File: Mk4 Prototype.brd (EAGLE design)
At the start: 121.6 x 80 mm, 223 parts, among them IC1 MSP432E401, IC10 TPD3E001DRL, IC11 LMV358ID, IC12 SN74HC4066D, IC13 TPA2006D1, IC2 AS4C4M16SA-7TCN, IC3 CC3120MOD, IC4 MCP23017ML, IC5 SIM800C, IC6 SST26VF016B-104I/SM, IC7 TPD3E001DRL, IC8 BQ25601, IC9 TPS62082, J1 78723-1001, J2 ER-CON50HT-1, J3 2x5 1.27mm, J4 GSM-COIL-ANT, J5 S2B-PH-SM4-TB(LF)(SN), Q1 2N7002PW, Q2 2N7002PW, Q3 CSD25402Q3A, Q8 CSD13202Q2, SW1 JOYSTICK, U1 ZX62-B-5PA(33), U4 MIC-4MM, U5 LDMS1540S-01-R8-0.8-R, X1 ABS07-32.768KHZ-T, X2 ABM8G-25.000MHZ-B4Y-T

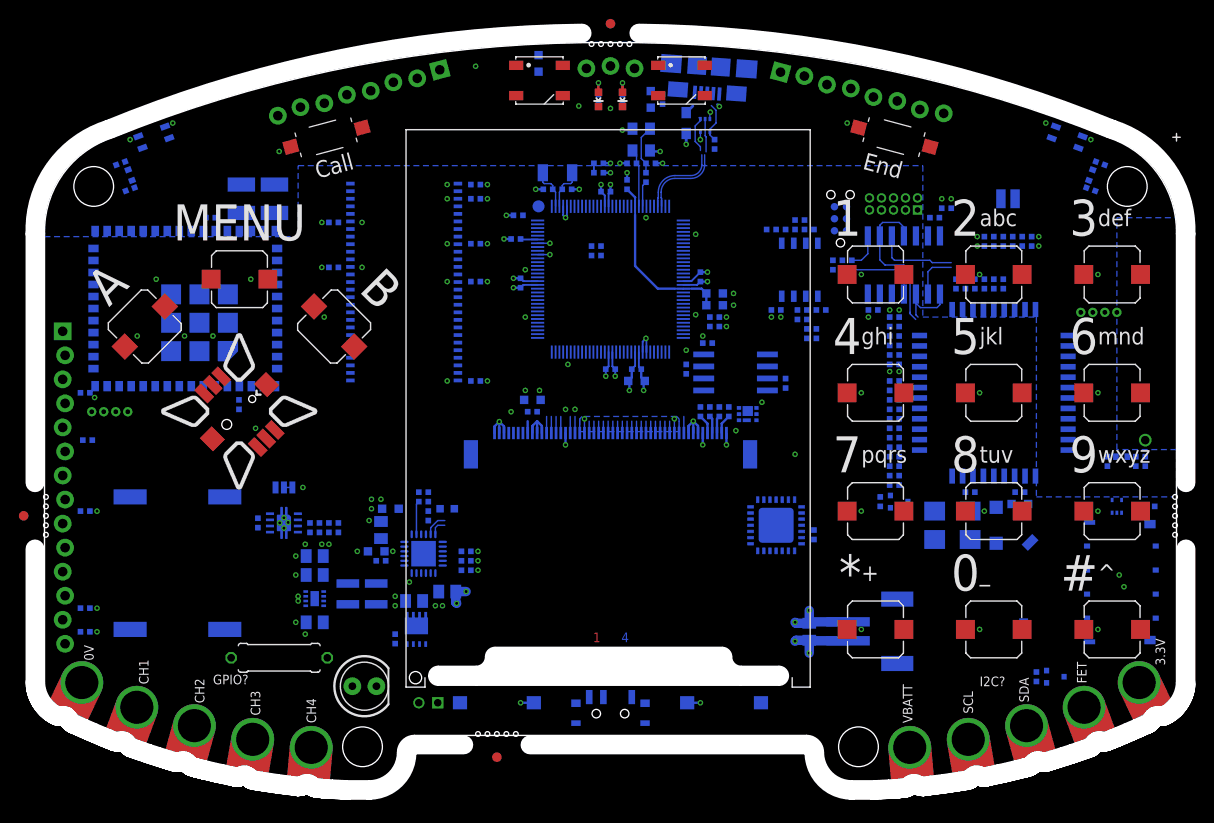
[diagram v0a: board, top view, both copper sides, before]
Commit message: Bom based updates
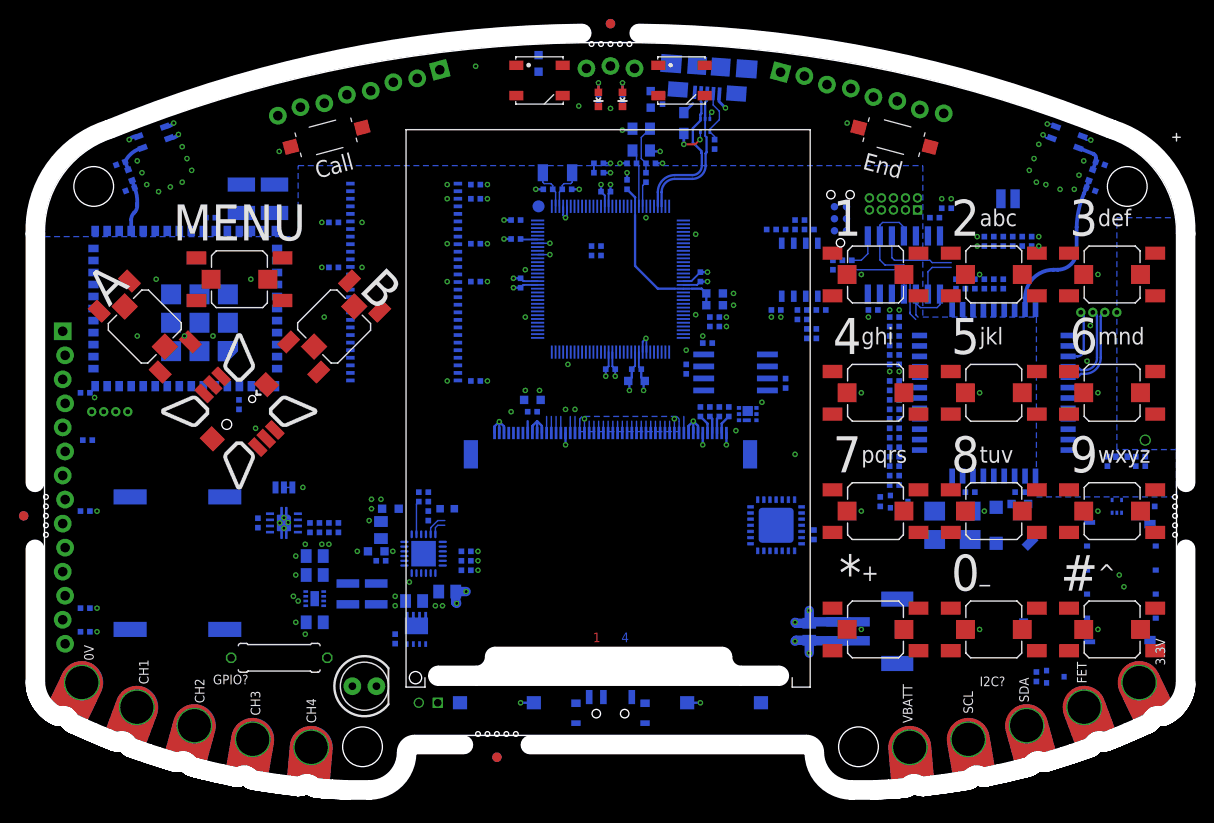
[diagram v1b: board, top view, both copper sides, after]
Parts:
- C1, C14, C41, C7: value 0603/1u/10V/X5R -> 0603/1u/6V3/X5R
- C20: value 0603/3300p/50V/X7R -> 0603/3n3/50V/X7R
- C48, C49, C50: value 0402/22p/10V/X5R -> 0402/22p/10V/C0G
- C52, C54, C55, C64, C66, C67: value 0402/33p/50V/X5R -> 0402/33p/50V/C0G
- C53, C56, C57, C65, C68, C69: value 0402/10p/50V/X5R -> 0402/10p/50V/C0G
- C6: value 0603/2u2/10V/X5R -> 0603/2u2/6V3/X5R
- S1, S10, S11, S12, S13, S14, S15, S2, S3, S4, S5, S6, S7, S8, S9: device TiLDA Mk4 Parts:SKPMAPE010 -> TiLDA Mk4 Parts:SKPMAPE010-COMBINED
- moved C52 1.00 mm to (42.0, 57.5)
- moved C53 1.00 mm to (40.0, 56.5)
- moved C54 1.00 mm to (44.0, 57.5)
- moved C55 1.00 mm to (40.0, 57.5)
- moved C56 1.00 mm to (42.0, 56.5)
- moved C57 1.00 mm to (44.0, 56.5)
- moved R5 0.56 mm to (-10.0, 59.2)
- moved L2 0.25 mm to (7.75, 69.5)
- turned S13 to 135 degrees
- turned S15 to 45 degrees
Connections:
- net N$1 renamed LED5_R
- net N$10 renamed AMP_IN_N
- net N$11 renamed AMP_IN_P
- net N$12 renamed AMP_IN_R_P
- net N$13 renamed BQ_STAT_R
- net N$14 renamed POWER_SWITCH
- net N$15 renamed AMP_IN_R_N
- net N$17 renamed BTST
- net N$19 renamed BQ_!QON
- net N$2 renamed MIC_PWM_AMP_+
- net N$3 renamed ETHLED0_R
- net N$4 renamed ETHLED1_R
- net N$5 renamed RBIAS+
- net N$51 renamed LED2_R
- net N$52 renamed LED1_R
- net N$6 renamed USB_SHIELD
- net N$64 renamed LEDK
- net N$7 renamed MIC_PWM_R
- net BTN_1: now also S1.B1, S1.B2
- net BTN_10: now also S10.B1, S10.B2
- net BTN_11: now also S11.B1, S11.B2
- net BTN_12: now also S12.B1, S12.B2
- net BTN_2: now also S2.B1, S2.B2
- net BTN_3: now also S3.B1, S3.B2
- net BTN_4: now also S4.B1, S4.B2
- net BTN_5: now also S5.B1, S5.B2
- net BTN_6: now also S6.B1, S6.B2
- net BTN_7: now also S7.B1, S7.B2
- net BTN_8: now also S8.B1, S8.B2
- net BTN_9: now also S9.B1, S9.B2
- net BTN_A: now also S13.B1, S13.B2
- net BTN_B: now also S15.B1, S15.B2
- net BTN_MENU: now also S14.B1, S14.B2
- net GND: now also S1.A1, S1.A2, S10.A1, S10.A2, S11.A1, S11.A2, S12.A1, S12.A2, S13.A1, S13.A2, S14.A1, S14.A2, S15.A1, S15.A2, S2.A1, S2.A2, S3.A1, S3.A2, S4.A1, S4.A2, S5.A1, S5.A2, S6.A1, S6.A2, S7.A1, S7.A2, S8.A1, S8.A2, S9.A1, S9.A2
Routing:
- net BT_ANT: track 0.00 -> 16.3 mm
- net SIM_D_N: track 0.00 -> 9.28 mm
- net SIM_D_P: track 0.00 -> 8.72 mm
- net GND: track 72.5 -> 80.1 mm, vias 106 -> 128
- net SIM_VBUS: track 0.00 -> 6.05 mm
- net WIFI_ANT: track 0.00 -> 5.54 mm
- net BT_ANT_L: track 0.00 -> 3.50 mm
- net USB_D_N: track 12.4 -> 15.8 mm
- net USB_D_P: track 11.9 -> 15.2 mm
- net WFIF_ANT_L: track 0.00 -> 3.26 mm
- net VBUS: track 1.98 -> 3.90 mm
- net USB_ID_R: track 4.28 -> 5.75 mm

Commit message: Connect some pins, try out TI Booster pack headers and add MIC disconnect
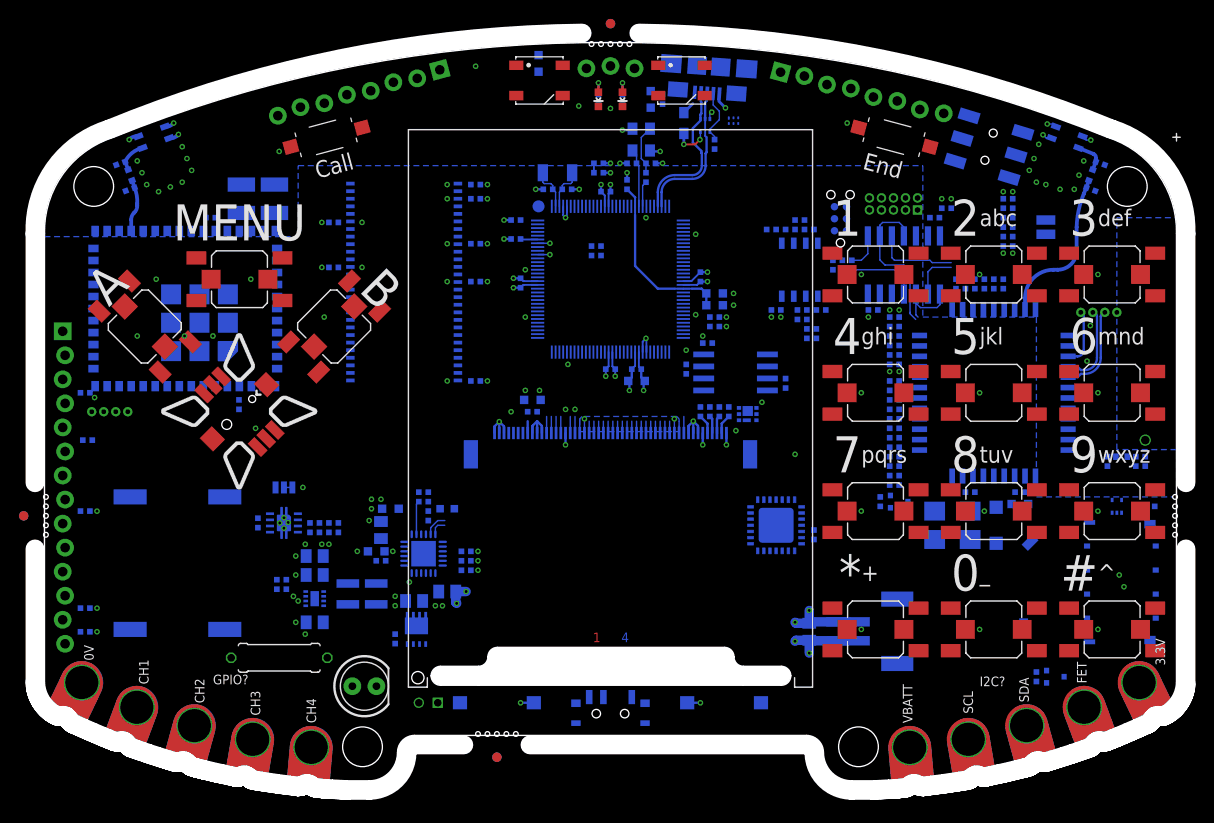
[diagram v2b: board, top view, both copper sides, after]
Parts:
- added IC14: TPD4S012, TiLDA Mk4 Parts:SON-6
- added R60, R61: (no value), TiLDA Mk4 Parts:R0402-SMALLER
- added S22: AYZ0202AGRLC, TiLDA Mk4 Parts:AYZ-JS-COMBINED
- moved U4 5.00 mm to (46.0, 58.5), turned to 90 degrees
- moved C53 4.74 mm to (41.5, 61.0), turned to 90 degrees
- moved C55 4.30 mm to (42.5, 61.0), turned to 90 degrees
- moved C56 2.55 mm to (41.5, 59.0), turned to 90 degrees
- moved C57 2.55 mm to (41.5, 57.0), turned to 270 degrees
- moved C52 1.58 mm to (42.5, 59.0), turned to 90 degrees
- moved C54 1.58 mm to (42.5, 57.0), turned to 270 degrees
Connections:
- net PD0 renamed CC_MISO
- net PD1 renamed CC_MOSI
- net PD2 renamed CC_!CS
- net PD3 renamed CC_CLK
- net PD4 renamed CC_TX
- net PD5 renamed CC_RX
- net PE1 renamed CC_!HIB
- net PJ0 renamed SIM_TX
- net PJ1 renamed SIM_RX
- net PK0 renamed CC_!RST
- removed net PA0: IC1.33
- removed net PA1: IC1.34
- removed net PD7: IC1.128
- removed net PE0: IC1.15
- removed net PE4: IC1.123
- removed net PE5: IC1.124
- removed net PF3: IC1.45
- removed net PN1: IC1.108
- removed net PN2: IC1.109
- removed net PP4: IC1.105
- removed net PP5: IC1.106
- removed net PQ4: IC1.102
- new net MIC_SWITCHED_N: IC12.10, S22.5
- new net MIC_SWITCHED_P: IC12.2, S22.2
- new net TPS_FB: IC9.4, R60.2, R61.1
- new net VCC: IC14.4
- net 3V3: now also R60.1
- net BQ_!INT: now also IC1.124
- net BTN_MENU: now also IC1.34
- net CC_IRQ: now also IC1.15
- net GND: now also IC14.6, R61.2
- net MCP_INT: now also IC1.33
- net MIC_N: now also S22.6; no longer IC12.10
- net MIC_P: now also S22.3; no longer IC12.2
- net MIC_PWM: now also IC1.45
- net MUX_A: now also IC1.108
- net MUX_B: now also IC1.109
- net NETLIGHT: now also IC1.105
- net PWR_KEY: now also IC1.106
- net SIM_STATUS: now also IC1.102
- net SPK_ADC: now also IC1.128
- net WS2812: now also IC1.123
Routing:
- net MIC_SWITCHED_N: track 0.00 -> 8.79 mm
- net MIC_N: track 8.79 -> 0.00 mm
- net MIC_SWITCHED_P: track 0.00 -> 5.01 mm
- net MIC_P: track 5.01 -> 0.00 mm
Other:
- board text added: "MIC"

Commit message: Night 4, Swap out CC3120MOD for CC3130R Getting some routing done
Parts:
- added C100, C101, C98, C99: 0402/12p/50V/C0G, TiLDA Mk4 Parts:C0402-SMALLER
- added C59, C60, C61, C62, C91, C92, C94, C95, C96, C97: 0402/100n/10V/X5R, TiLDA Mk4 Parts:C0402-SMALLER
- added C63, C87, C93: 0805/10u/10V/X5R, TiLDA Mk4 Parts:C0805-N
- added C84, C85: 0603/22u/4V/X5R, TiLDA Mk4 Parts:C0603K-SMALL
- added C86: 0402/1u/10V/X5R, TiLDA Mk4 Parts:C0402-SMALLER
- added C88, C89, C90: 0603/4u7/10V/X5R, TiLDA Mk4 Parts:C0603K-SMALL
- added FL1: DEA202450BT-1294C1-H, TiLDA Mk4 Parts:DEA202450BT
- added IC15: CC3120R, TiLDA Mk4 Parts:VQFN-64
- added L7, L9: LQM2HPN2R2MG0L, TiLDA Mk4 Parts:1008
- added L8: LQM2HPN1R0MG0L, TiLDA Mk4 Parts:1008
- added R62, R66: 0402/10K/5%, TiLDA Mk4 Parts:R0402-SMALLER
- added R63, R64, R65, R67, R68, R69, R70, R71, R72, R73: 0402/100K/5%, TiLDA Mk4 Parts:R0402-SMALLER
- added X3: ABS07-32.768KHZ-T, TiLDA Mk4 Parts:RESONATOR_EPSON_FC_145
- added X4: ABM8G-40.000MHZ-4Y-T3, TiLDA Mk4 Parts:CRYSTAL-3.2-2.5
- ANT1: device TiLDA Mk4 Parts:2450AT18D0100-RIGHT -> TiLDA Mk4 Parts:2450AT18D0100
- IC3: value CC3120MOD -> MX25R1635FM1IL0; device TiLDA Mk4 Parts:CC3100MOD-LWK -> TiLDA Mk4 Parts:SO08-EIAJ
- IC4: value MCP23017ML -> TCA9555; device TiLDA Mk4 Parts:QFN28-ML_6X6MM -> TiLDA Mk4 Parts:QFN-24
- moved R23 60.5 mm to (39.2, 11.8), turned to 90 degrees
- moved R24 59.1 mm to (38.2, 11.8), turned to 90 degrees
- moved ANT1 49.8 mm to (-58.4, 19.2), turned to 270 degrees
- moved C43 48.5 mm to (-37.8, 13.0), turned to 0 degrees
- moved C77 42.1 mm to (-57.5, 23.5), turned to 270 degrees
- moved L6 41.3 mm to (-56.0, 23.0), turned to 0 degrees
- moved C76 39.2 mm to (-54.2, 23.5), turned to 270 degrees
- moved SJ1 31.2 mm to (-31.0, 62.0), turned to 180 degrees
- moved U5 30.1 mm to (-44.0, 53.0)
- moved C44 29.5 mm to (-45.8, 30.2), turned to 90 degrees
- moved C58 27.1 mm to (-34.5, 54.2)
- moved IC3 25.4 mm to (-29.5, 29.8)
- moved JP8 25.1 mm to (-49.2, 14.0), flipped to the top, turned to 180 degrees
- moved C42 24.3 mm to (-34.0, 37.2)
- moved R25 23.4 mm to (-35.0, 16.8), turned to 180 degrees
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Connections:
- net LCD_BLIGHT renamed PWM0_LCD_BLIGHT
- net LCD_CLK renamed SSI0_LCD_CLK
- net LCD_CS renamed SSI0_LCD_CS
- net LCD_MISO renamed SSI0_LCD_MISO
- net LCD_MOSI renamed SSI0_LCD_MOSI
- net MIC_PWM renamed PWM3_MIC_PWM
- net NETLIGHT renamed SIM_NETLIGHT
- net PD6 renamed AIN5_PD6
- net PWR_KEY renamed SIM_PWR_KEY
- net SPK_ADC renamed AIN4_SPK_ADC
- removed net !CC_HIB: IC3.4, R25.1
- removed net !CC_RST: IC3.35
- removed net ADC_X: J2.46
- removed net ADC_Y: J2.47
- removed net CC_!CS: IC1.3
- removed net CC_!RST: IC1.18
- removed net CC_CLK: IC1.4
- removed net CC_MISO: IC1.1
- removed net CC_MOSI: IC1.2
- removed net CC_RX: IC1.126
- removed net CC_TX: IC1.125
- removed net PE2: IC1.13
- removed net PE3: IC1.12
- removed net PF1: IC1.43
- removed net PF2: IC1.44
- removed net PK7: IC1.60
- removed net PL4: IC1.85
- removed net PM6: IC1.72
- removed net SPI1_MISO: IC3.7
- removed net SPI1_MOSI: IC3.6
- removed net SPI1_NSS: IC3.8
- removed net SPI1_SCK: IC3.5
- removed net SSI3DAT3: IC1.119
- removed net USART1_RX: IC3.46
- removed net USART1_TX: IC3.47
- new net AIN0_ADC_X: IC1.13, J2.46
- new net AIN1_ADC_Y: IC1.12, J2.47
- new net CC_!CTS: IC15.61
- new net CC_!RESET: C60.2, IC1.18, IC15.32, R73.1
- new net CC_!RTS: IC15.50, R70.1
- new net CC_RCT_XTAL_N: C100.2, IC15.52, X3.P$1
- new net CC_RESERVED@19: IC15.19, R65.1
- new net CC_RTC_XTAL_P: C101.2, IC15.51, X3.P$2
- new net CC_WLAN_XTAL_: C99.2, IC15.22, X4.3
- new net CC_WLAN_XTAL_P: C98.2, IC15.23, X4.1
- new net DCDC_ANA2_SW_N: IC15.46
- new net DCDC_ANA2_SW_P: IC15.45
- new net DCDC_ANA_SW: IC15.38, L7.2
- new net DCDC_DIG_SW: IC15.43, L9.2
- new net DCDC_PA_SW_N: IC15.41, L8.1
- new net DCDC_PA_SW_P: IC15.40, L8.2
- new net FLASH_PU: IC3.3, IC3.7, R66.2
- new net SOP0: IC15.35, R64.1
- new net SOP1: IC15.34, R63.1
- new net SOP2: IC15.21, R62.1
- new net SSI2_CC_!CS: IC1.3, IC15.8
- new net SSI2_CC_CLK: IC1.4, IC15.5
- new net SSI2_CC_MISO: IC1.1, IC15.7, R71.1
- new net SSI2_CC_MOSI: IC1.2, IC15.6
- new net UART2_RX: IC1.125, IC15.55, R68.1
- new net UART2_TX: IC1.126, IC15.57, R69.1
- new net VDD_ANA: C44.1, C61.1, C62.1, C63.1, IC15.25, IC15.36, IC15.48, L7.1
- new net VDD_DIG_CC: C87.1, C96.1, C97.1, IC15.56, IC15.9, L9.1
- new net VDD_PA: C84.1, C85.1, C86.1, IC15.33, IC15.42
- new net VDD_PLL: C94.1, IC15.24
- new net VDD_RAM: C95.1, IC15.49
- new net WIFI_ANT_F: FL1.IN, IC15.31
- net 3V3: now also C59.2, C88.1, C89.1, C90.1, C91.1, C92.1, C93.1, IC15.10, IC15.37, IC15.39, IC15.44, IC15.47, IC15.54, IC3.8, IC4.21, R66.1, R67.2, R68.2, R69.2, R73.2; no longer C44.2, IC3.36, IC3.37, IC3.40, IC4.5
- net BTN_1: now also IC4.1; no longer IC4.17
- net BTN_10: now also IC4.11; no longer IC4.26
- net BTN_11: now also IC4.12; no longer IC4.27
- net BTN_12: now also IC4.13; no longer IC4.28
- net BTN_2: now also IC4.2; no longer IC4.18
- net BTN_3: now also IC4.3; no longer IC4.19
- net BTN_4: now also IC4.4; no longer IC4.20
- net BTN_5: now also IC4.5; no longer IC4.21
- net BTN_6: now also IC4.6; no longer IC4.22
- net BTN_7: now also IC4.7; no longer IC4.23
- net BTN_8: now also IC4.8; no longer IC4.24
- net BTN_9: now also IC4.10; no longer IC4.25
- net BTN_A: now also IC4.16; no longer IC4.3
- net BTN_B: now also IC4.17; no longer IC4.4
- net BTN_CALL: now also IC4.14; no longer IC4.1
- net BTN_END: now also IC4.15; no longer IC4.2
- net CC_!HIB: now also IC15.2, R25.1
- net CC_IRQ: now also IC15.15, R72.1; no longer IC3.11
- net FET: now also IC1.85
- net FLASH_!CS: now also IC15.14, IC3.1, R67.1; no longer IC3.14
- net FLASH_CLK: now also IC15.11, IC3.6; no longer IC3.15
- net FLASH_MISO: now also IC15.13, IC3.2; no longer IC3.13
- net FLASH_MOSI: now also IC15.12, IC3.5; no longer IC3.17
- net GND: now also ANT1.4, C100.1, C101.1, C44.2, C59.1, C60.1, C61.2, C62.2, C63.2, C84.2, C85.2, C86.2, C87.2, C88.2, C89.2, C90.2, C91.2, C92.2, C93.2, C94.2, C95.2, C96.2, C97.2, C98.1, C99.1, FL1.GND@2, FL1.GND@4, IC15.PAD, IC3.4, IC4.18, IC4.23, IC4.24, IC4.25, IC4.9, R62.2, R63.2, R64.2, R65.2, R70.2, R71.2, R72.2, X4.2, X4.4; no longer ANT1.1, C44.1, IC3.1, IC3.16, IC3.2, IC3.27, IC3.28, IC3.30, IC3.32, IC3.38, IC3.43, IC3.55, IC3.56, IC3.57, IC3.58, IC3.59, IC3.60, IC3.61, IC3.62, IC3.63, IC4.11, IC4.12, IC4.13, IC4.6
- net I2C5_SCL: now also IC4.19; no longer IC4.8
- net I2C5_SDA: now also IC4.20; no longer IC4.9
- net LED1: now also IC1.43; no longer IC1.95
- net LED2: now also IC1.44; no longer IC1.96
- net MCP_INT: now also IC4.22; no longer IC4.16
- net SSI3_DAT3: now also IC1.119
- net T_X: now also IC1.60
- net T_Y: now also IC1.72
- net USB_ID: now also IC1.95
- net VBUS: now also IC1.96
- net WFIF_ANT_L: now also ANT1.1; no longer ANT1.4
- net WIFI_ANT: now also FL1.OUT; no longer IC3.31
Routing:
- net GND: track 80.1 -> 371.4 mm, vias 128 -> 288
- net VBATT: track 0.00 -> 108.7 mm, vias 0 -> 11
- net 3V3: track 34.0 -> 130.6 mm, vias 39 -> 63
- net FET_OUT: track 0.00 -> 90.7 mm
- net V_UNREG: track 0.00 -> 78.7 mm, vias 0 -> 4
- net VBUS: track 3.90 -> 82.5 mm, vias 2 -> 6
- net EN0RXI_N: track 0.00 -> 74.7 mm
- net EN0RXI_P: track 0.00 -> 69.2 mm
- net EN0TXO_N: track 0.00 -> 63.2 mm
- net EN0TXO_P: track 0.00 -> 62.7 mm
- net BTN_A: track 0.00 -> 61.2 mm
- net ETHLED1: track 0.00 -> 60.9 mm, vias 0 -> 1
- net BTN_MENU: track 0.00 -> 59.6 mm
- net ETHLED0: track 0.00 -> 53.2 mm, vias 0 -> 1
- net SDRAM_CKE: track 0.00 -> 51.1 mm, vias 0 -> 2
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- added copper zone on layer 16, net 3V3
- added copper zone on layer 16, net BQ_SW
- added copper zone on layer 16, net LEDK
- added copper zone on layer 15, net N$1
- added copper zone on layer 15, net N$2
- added copper zone on layer 15, net N$3
- added copper zone on layer 16, net SW
- added copper zone on layer 16, net VBAT
- added copper zone on layer 2, net VBAT
- added copper zone on layer 16, net VBATT
- added copper zone on layer 2, net VBATT
- added copper zone on layer 16, net VBUS
- added copper zone on layer 2, net VDD_ANA
- added copper zone on layer 2, net VDD_PA
- added copper zone on layer 16, net V_UNREG
